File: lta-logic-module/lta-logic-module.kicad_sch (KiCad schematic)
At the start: 7 parts, among them J1 Conn_01x01_Female, J2 Conn_01x01_Female, U1 Feather_M4_Express

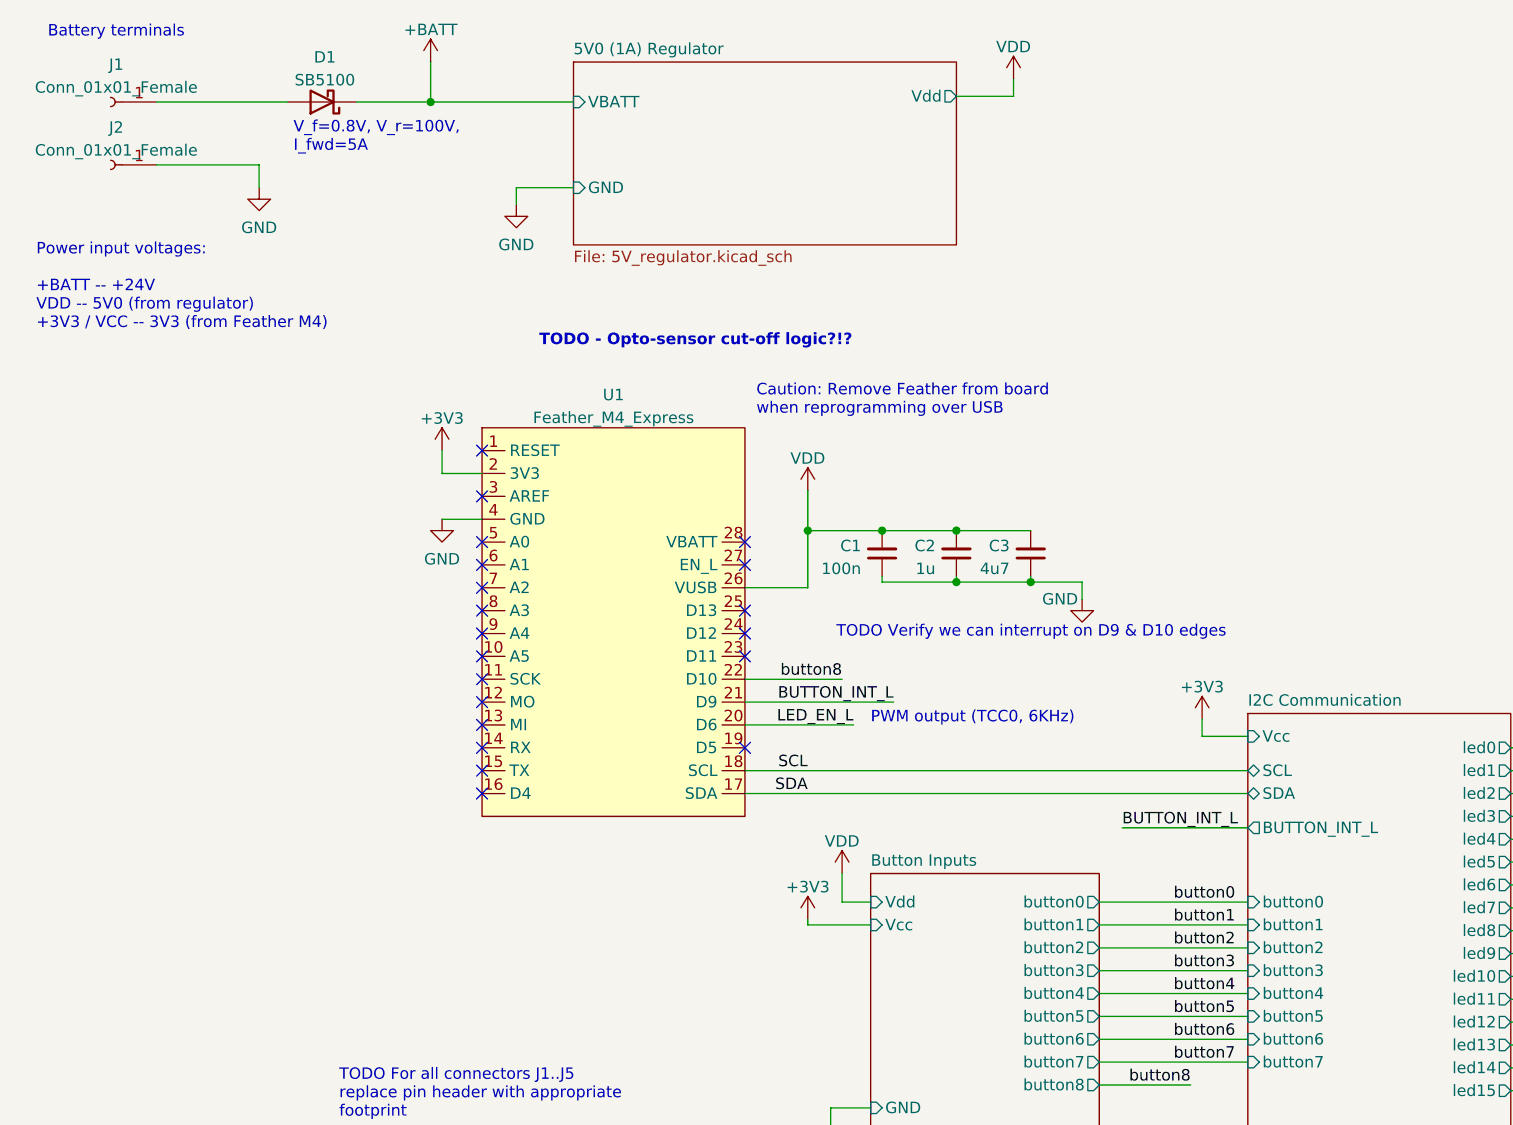
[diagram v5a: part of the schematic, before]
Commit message: Add light sensor circuit.
Adjust TODOs and comments after testing btn circuit.
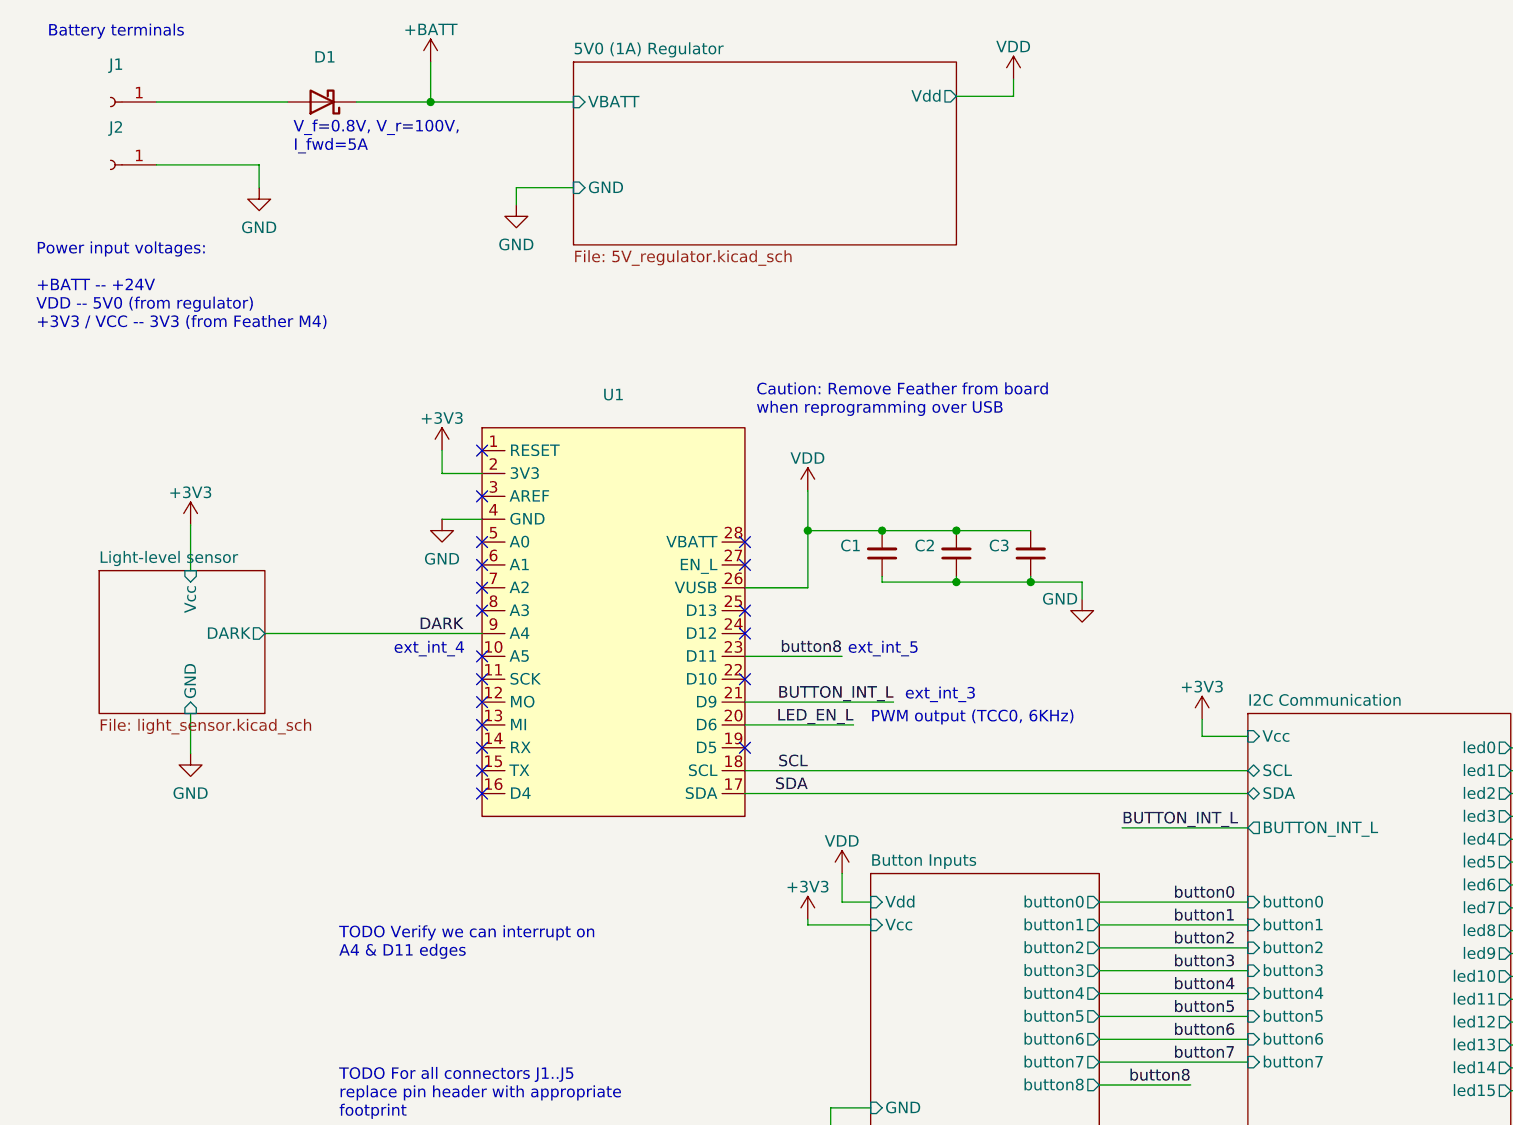
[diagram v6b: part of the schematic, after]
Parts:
- C1: value 100n -> (none); footprint Capacitor_SMD:C_0603_1608Metric -> (none)
- C2: value 1u -> (none); footprint Capacitor_SMD:C_0603_1608Metric -> (none)
- C3: value 4u7 -> (none); footprint Capacitor_SMD:C_0805_2012Metric -> (none)
- D1: value SB5100 -> (none); footprint Diode_THT:D_DO-201AD_P15.24mm_Horizontal -> (none)
- J1, J2: value Conn_01x01_Female -> (none); footprint Connector_PinHeader_2.54mm:PinHeader_1x01_P2.54mm_Vertical -> (none)
- U1: value Feather_M4_Express -> (none); footprint aaron-imported-parts:Arduino_Feather_M4_Express_PinHeaders -> (none)
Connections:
- net button8: now also U1.23 (D11); no longer U1.22 (D10)
- net DARK: now reaches U1.9 (A4)
- no-connect marks 20 -> 19
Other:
- added sheet Light-level sensor (light_sensor.kicad_sch)
- note added: "TODO Verify we can interrupt on A4 & D11 edges"
- note added: "ext_int_3"
- note added: "ext_int_4"
- note added: "ext_int_5"
- note removed: "TODO - Opto-sensor cut-off logic?!?"
- note removed: "TODO Verify we can interrupt on D9 & D10 edges"

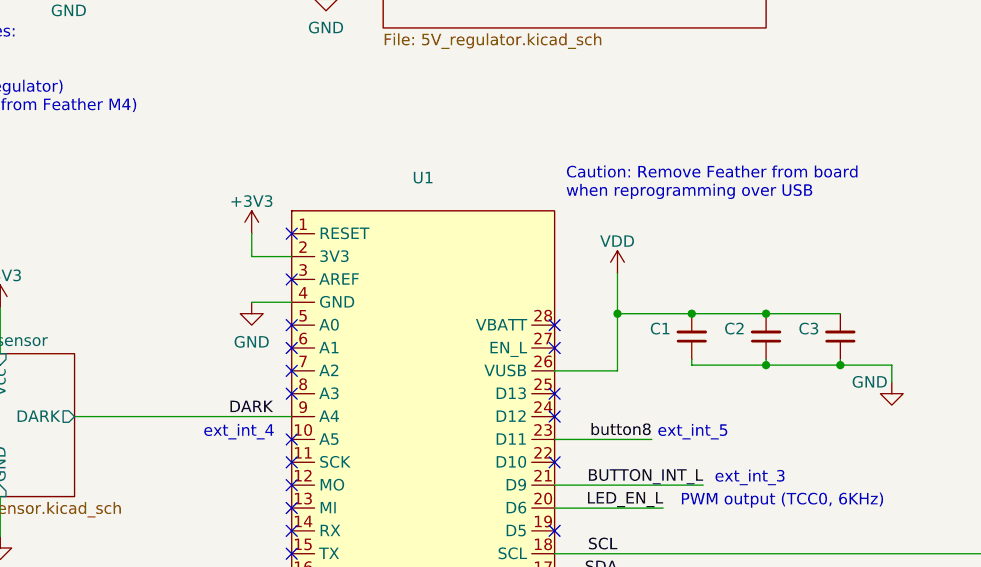
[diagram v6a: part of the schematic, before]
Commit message: Add main draft of PCB layout for logic module.
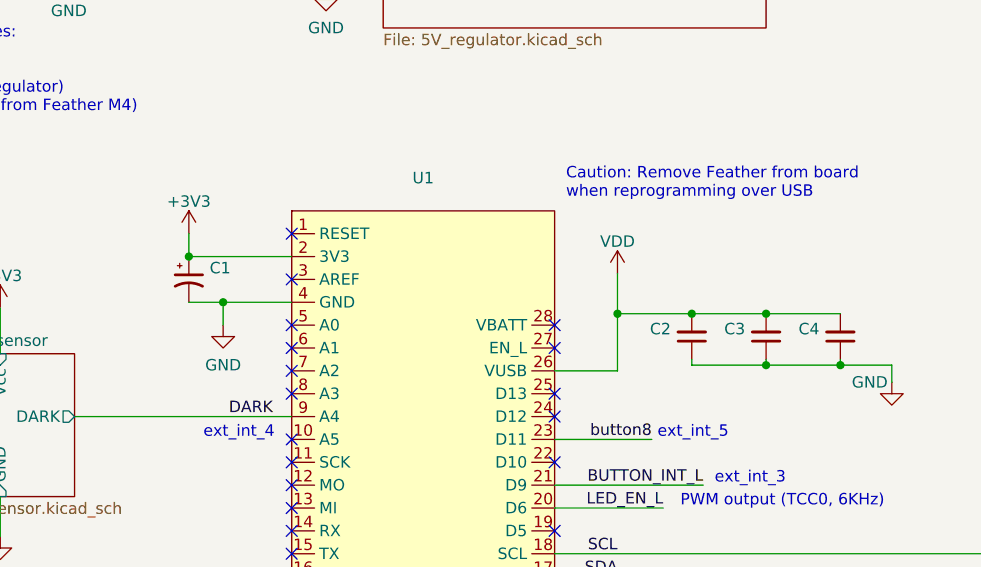
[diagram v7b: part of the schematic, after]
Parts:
- added C1: (no value), symbol Device:C_Polarized_Small_US
- D1: Comment (none) -> Any 100V 5A Schottky diode, Vf <= 850mV
- renumbered C1 to C2, C2 to C3, C3 to C4
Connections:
- net +3V3: now also C1.1
- net GND: now also C1.2

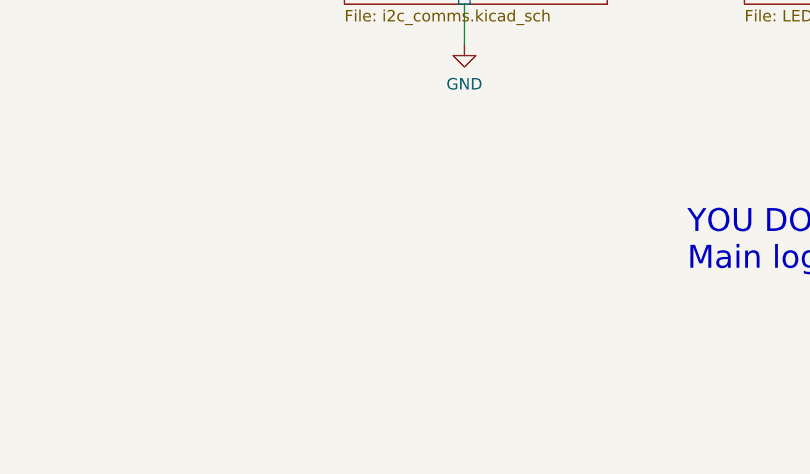
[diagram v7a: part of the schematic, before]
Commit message: Fix all the footprint data.
Somehow my footprint info got clobbered. Reset a bunch of symbol
properties to empty... this info is now all back in place.

* Added 3 fiducial marks
* Added 4 mounting holes
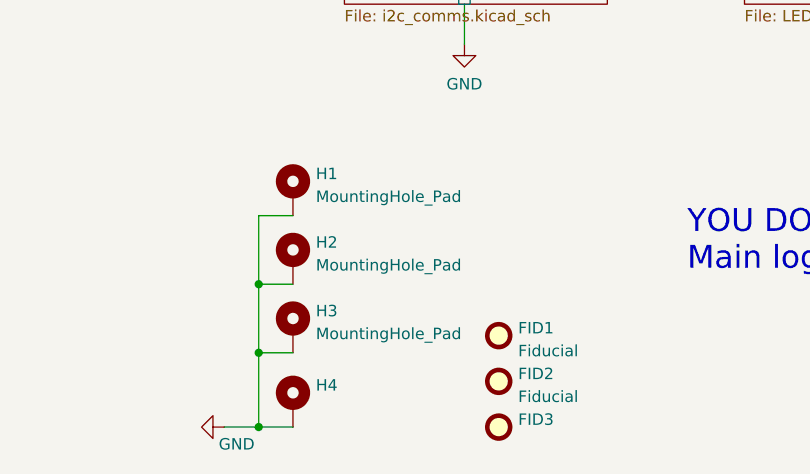
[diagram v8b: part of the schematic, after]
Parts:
- added FID1, FID2: Fiducial, Fiducial:Fiducial_1mm_Mask2mm, symbol Mechanical:Fiducial
- added FID3: (no value), symbol Mechanical:Fiducial
- added H1, H2, H3: MountingHole_Pad, MountingHole:MountingHole_2.2mm_M2_ISO7380_Pad, symbol Mechanical:MountingHole_Pad
- added H4: (no value), symbol Mechanical:MountingHole_Pad
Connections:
- net GND: now also H1.1, H2.1, H3.1, H4.1
